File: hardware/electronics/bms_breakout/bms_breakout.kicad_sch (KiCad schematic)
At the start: 67 parts, among them J1 Conn_01x03_Socket, Q1 BUK961R6-40E, Q2 VAL, Q3 VAL, U1 BQ76905, U2 BQ25798RQMR

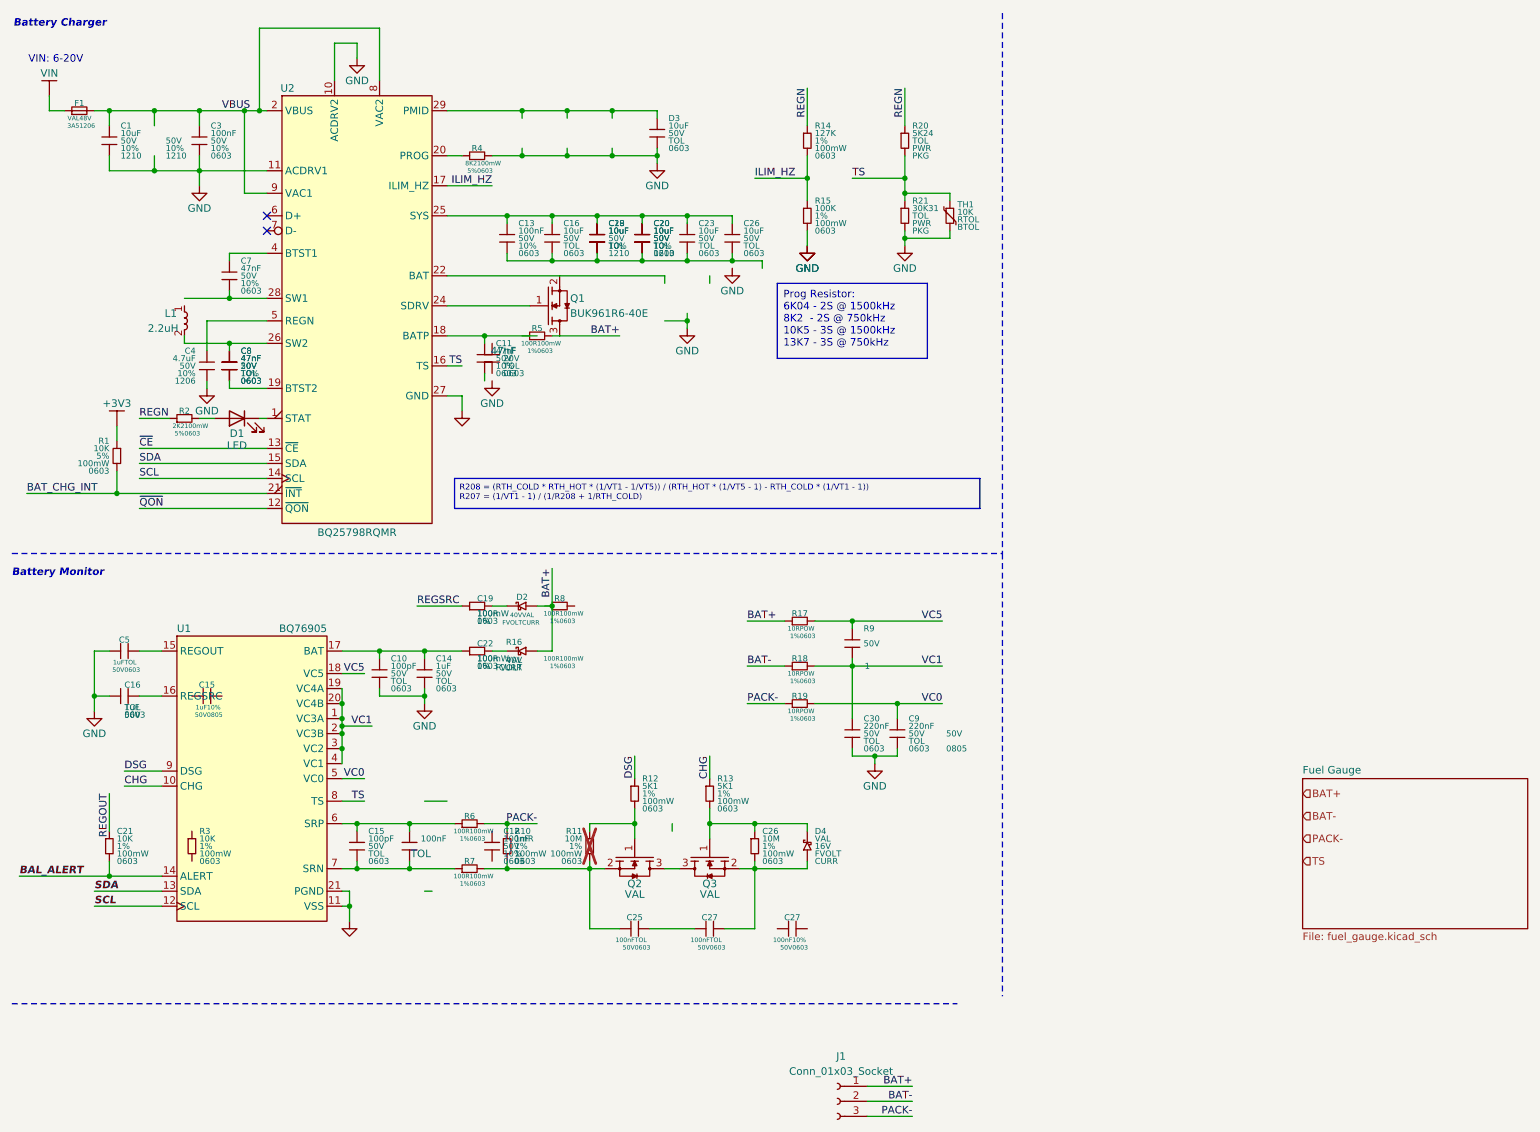
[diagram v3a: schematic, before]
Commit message: formatted for hierarchical sheets
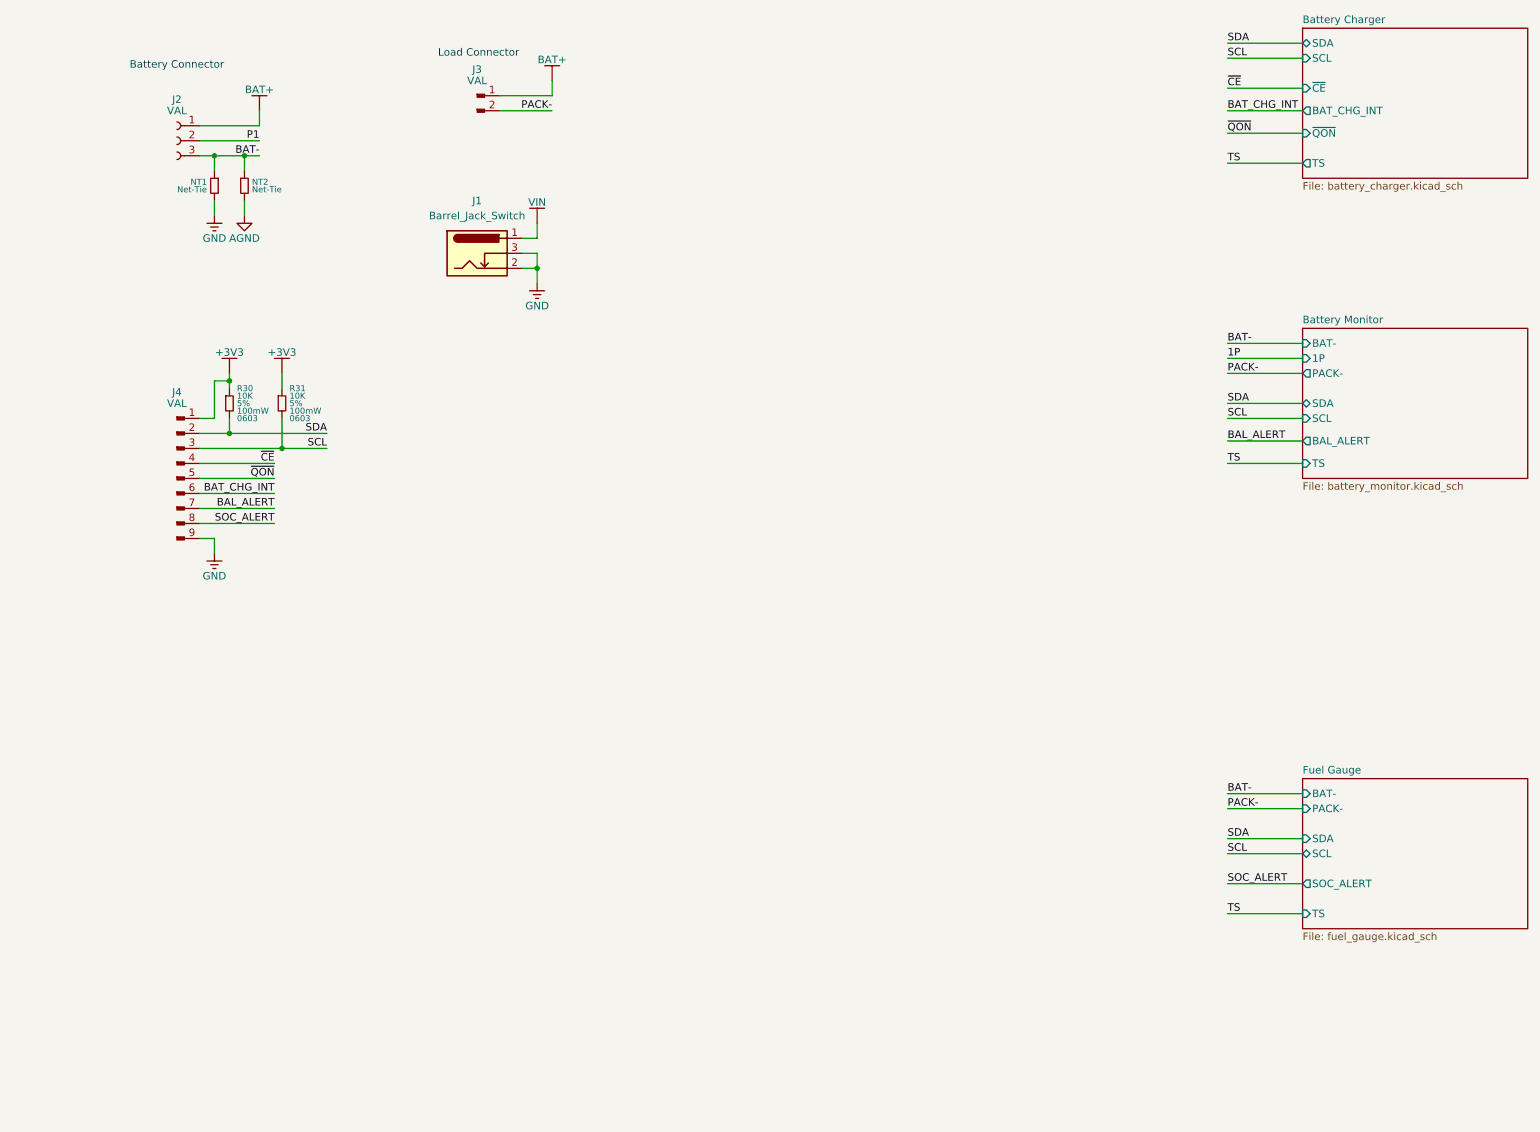
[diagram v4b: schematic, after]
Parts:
- removed #PWR02: 100nF, symbol DSE-Passives:C
- removed C1, C16, C18, C20 (x2), C23, C26, C29, D3: 10uF, symbol DSE-Passives:C
- removed C10, C15: 100pF, symbol DSE-Passives:C
- removed C11, C8: 47nF, symbol DSE-Passives:C
- removed C11, C7, C8: 47nF, DSE-Capacitors-SMD:CAPC160X80X88L35N, symbol DSE-Passives:C
- removed C12, C13, C3: 100nF, DSE-Capacitors-SMD:CAPC160X80X88L35N, symbol DSE-Passives:C
- removed C14: 1uF, symbol DSE-Passives:C
- removed C15: 1uF, DSE-Capacitors-SMD:CAPC200X125X88L50N, symbol DSE-Passives:C_horizontal
- removed C16, C5: 1uF, symbol DSE-Passives:C_horizontal
- removed C19, C22, R6, R7: 100R, symbol DSE-Passives:R_horizontal
- removed C21: 10K, symbol DSE-Passives:R
- removed C25, C27: 100nF, symbol DSE-Passives:C_horizontal
- removed C26, R11: 10M, symbol DSE-Passives:R
- removed C27: 100nF, DSE-Capacitors-SMD:CAPC160X80X88L35N, symbol DSE-Passives:C_horizontal
- removed C30, C9: 220nF, symbol DSE-Passives:C
- removed C4: 4.7uF, DSE-Capacitors-SMD:CAPC320X160X88L50N, symbol DSE-Passives:C
- removed D1: LED, symbol Device:LED
- removed D2, R16: VAL, symbol DSE-Passives:D_Schottky_horizontal
- removed D4: VAL, symbol DSE-Passives:D_Schottky
- removed F1: VAL, symbol DSE-Passives:F_horizontal
- removed J1: Conn_01x03_Socket, symbol Connector:Conn_01x03_Socket
- removed L1: 2.2uH, symbol DSE-Passives:L
- removed Q1: BUK961R6-40E, symbol DSE-Transistors:NMOS_GSD
- removed Q2, Q3: VAL, symbol DSE-Transistors:NMOS_GSD
- removed R1, R3: 10K, DSE-Resistors-SMD:RESC160X80X55L30N, symbol DSE-Passives:R
- removed R10: 1mR, symbol DSE-Passives:R
- removed R12, R13: 5K1, symbol DSE-Passives:R
- removed R14: 127K, DSE-Resistors-SMD:RESC160X80X55L30N, symbol DSE-Passives:R
- removed R15: 100K, DSE-Resistors-SMD:RESC160X80X55L30N, symbol DSE-Passives:R
- removed R17, R18, R19: 10R, symbol DSE-Passives:R_horizontal
- removed R2: 2K2, DSE-Resistors-SMD:RESC160X80X55L30N, symbol DSE-Passives:R_horizontal
- removed R20: 5K24, DSE-Resistors-SMD:RESC160X80X55L30N, symbol DSE-Passives:R
- removed R21: 30K31, DSE-Resistors-SMD:RESC160X80X55L30N, symbol DSE-Passives:R
- removed R4: 8K2, DSE-Resistors-SMD:RESC160X80X55L30N, symbol DSE-Passives:R_horizontal
- removed R5, R8: 100R, DSE-Resistors-SMD:RESC160X80X55L30N, symbol DSE-Passives:R_horizontal
- removed R9: 100R, DSE-Resistors-SMD:RESC160X80X55L30N, symbol DSE-Passives:C
- removed TH1: 10K, symbol DSE-Passives:Thermistor
- removed U1: BQ76905, symbol DSE-PMIC:BQ76905
- removed U2: BQ25798RQMR, symbol DSE-PMIC:BQ25798
- added J1: Barrel_Jack_Switch, symbol DS-Connectors:Barrel_Jack_Switch
- added J2: VAL, symbol DS-Connectors:Conn_01x03_Socket
- added J3: VAL, symbol DS-Connectors:Conn_01x02_Pin
- added J4: VAL, symbol DS-Connectors:Conn_01x09_Pin
- added NT1, NT2: Net-Tie, symbol DS-Passives:NT
- added R30, R31: 10K, symbol DS-Passives:R
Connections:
- net +3V3: now also J4.1, R30.1, R31.1
- net BAL_ALERT: now also J4.7
- net BAT+: now also J2.1, J3.1
- net BAT-: now also J2.3, NT1.1, NT2.1
- net BAT_CHG_INT: now also J4.6
- net GND: now also J1.2, J1.3, J4.9, NT1.2
- net PACK-: now also J3.2
- net SCL: now also J4.3, R31.2
- net SDA: now also J4.2, R30.2
- net VIN: now also J1.1
- net ~{CE}: now also J4.4
- net ~{QON}: now also J4.5
- new net AGND: NT2.2
- new net P1: J2.2
- new net SOC_ALERT: J4.8
- no-connect marks 2 -> 0
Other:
- added sheet Battery Charger (battery_charger.kicad_sch)
- added sheet Battery Monitor (battery_monitor.kicad_sch)
- sheet Fuel Gauge ports: added BAT-, PACK-, SCL, SDA, SOC_ALERT, TS; removed none
- note added: "Battery Connector"
- note added: "Load Connector"
- note removed: "Battery Charger"
- note removed: "Battery Monitor"
- note removed: "VIN: 6-20V"

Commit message: added footprints for all resistors and capacitors
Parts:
- R30, R31: footprint (none) -> DS-Resistors-SMD:CRCW0603
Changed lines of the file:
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@@
 			)
 		)
-		(property "Footprint" ""
+		(property "Footprint" "DS-Resistors-SMD:CRCW0603"
 			(at 55.88 73.66 0)
 			(effects
@@
 			)
 		)
-		(property "Footprint" ""
+		(property "Footprint" "DS-Resistors-SMD:CRCW0603"
 			(at 46.99 73.66 0)
 			(effects
